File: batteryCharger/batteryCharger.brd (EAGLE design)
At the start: 44.1 x 67 mm, 73 parts, among them J1 B4P-VH(LF)(SN), Q1 SIR414DP-T1-GE3, Q2 SI7635DP-T1-GE3, Q3 SI7635DP-T1-GE3, Q4 SIR414DP-T1-GE3, Q5 SI7635DP-T1-GE3

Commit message: final board file
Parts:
- added R21, R22, R23: (no value), pot:3223W
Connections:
- removed net N$11: R5.1, RN2.7, TM1.1
- removed net N$9: R19.1, RN2.8, TM3.1
- new net ACSET_TRIM: R19.1, R23.1, RN2.8, TM3.1
- new net ISET1_TRIM: R21.1, R5.1, RN2.7, TM1.1
- net ACSET: now also R23.2
- net GND: now also R21.3, R22.3, R23.3
- net ISET1: now also R21.2
- net ISET2: now also R22.2
- net VREF: now also R22.1
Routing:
- net N$9: track 35.3 -> 0.00 mm, vias 2 -> 0
- net ISET1_TRIM: track 0.00 -> 29.2 mm
- net N$11: track 27.5 -> 0.00 mm
- net ACSET_TRIM: track 0.00 -> 24.1 mm
- net GND: track 11.7 -> 13.1 mm, vias 120 -> 122
- net ISET1: track 38.6 -> 39.2 mm
- net VREF: track 111.8 -> 111.3 mm

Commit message: v2 with bug fixses
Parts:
- removed D2, D3: (no value), SparkFun-LED:LED-1206
- added DONE, PG: (no value), SparkFun-LED:LED-1206
- added R24: 10k, SparkFun-Resistors:0603
- moved U$3 9.60 mm to (3.30, 7.49)
- moved U$2 1.20 mm to (36.4, 4.06)
- moved R4 1.02 mm to (38.0, 13.3)
- moved Q5 0.92 mm to (17.7, 55.8), turned to 0 degrees
- moved D4 0.76 mm to (31.4, 36.6)
- moved Q3 0.67 mm to (23.0, 35.5), turned to 90 degrees
- moved Q1 0.57 mm to (18.4, 50.1)
- moved C7 0.51 mm to (28.8, 39.9)
- moved R7 0.46 mm to (21.6, 21.9)
- moved Q2 0.45 mm to (23.0, 27.9), turned to 270 degrees
- moved R8 0.38 mm to (29.0, 38.1)
- moved R14 0.36 mm to (38.0, 23.9)
- moved R1 0.28 mm to (28.8, 56.6)
- moved R5 0.25 mm to (38.0, 11.2)
- moved C6 0.25 mm to (24.0, 21.1)
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- renumbered D1 to CHARGING
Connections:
- removed net N$19: C5.1, Q2.5, Q2.6, Q2.7, Q2.8, Q2.9, Q3.5, Q3.6, Q3.7, Q3.8, Q3.9, R8.1, RN2.5
- new net N$11: C5.1, Q2.1, Q2.2, Q2.3, Q3.1, Q3.2, Q3.3, R8.1, RN2.5
- net ADAPTER: now also Q2.5, Q2.6, Q2.7, Q2.8, Q2.9; no longer Q2.1, Q2.2, Q2.3
- net GND: now also R24.2
- net N$10: now also R24.1
- net N$13: now also Q3.5, Q3.6, Q3.7, Q3.8, Q3.9; no longer Q3.1, Q3.2, Q3.3
- net N$5: now also DONE.A; no longer D2.A
- net N$6: now also PG.A; no longer D3.A
- net N$7: now also DONE.C; no longer D2.C
- net N$8: now also PG.C; no longer D3.C
- net OUTPUT: now also Q5.1, Q5.2, Q5.3; no longer Q5.5, Q5.6, Q5.7, Q5.8, Q5.9
- net PACK: now also Q5.5, Q5.6, Q5.7, Q5.8, Q5.9; no longer Q5.1, Q5.2, Q5.3
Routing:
- net N$11: track 0.00 -> 38.9 mm, vias 0 -> 2
- net N$19: track 35.4 -> 0.00 mm
- net PACK: track 85.5 -> 69.7 mm
- net ADAPTER: track 71.7 -> 57.7 mm
- net N$27: track 38.0 -> 31.1 mm, vias 2 -> 4
- net N$26: track 28.6 -> 22.2 mm
- net N$23: track 18.9 -> 21.0 mm
- net N$7: track 35.2 -> 36.6 mm
- net OUTPUT: track 45.4 -> 44.1 mm
- net N$5: track 3.06 -> 4.21 mm
- net N$17: track 28.7 -> 27.9 mm
- net N$22: track 6.28 -> 7.04 mm
- net N$21: track 2.25 -> 3.01 mm
- net N$14: track 121.9 -> 122.5 mm
- net N$6: track 2.09 -> 2.59 mm
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- added copper zone on layer 1, net N$11
- removed copper zone on layer 1, net N$19
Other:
- board text added: "INPUT C"
- board text added: "OUTPUT C"
- board text added: "V2.0"
- board text removed: "AC"
- board text removed: "CI"
- board text removed: "V1.0"

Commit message: Bug fixses
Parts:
- removed TP3, TP6: TPTP20SQ, testpad:TP20SQ
- added F2: SMD-MICRO-FUSE-BLOCK, f-lf-omniblok-s:OMNIBLOK
- R10, R9: value 10mOhm -> 0.01
- R17: value 100k -> 18k
- R18: value 30k -> 22.1k
- R19, R5: value 10k -> 18k
- R4: value 30k -> 32.4k
- moved R13 50.0 mm to (39.7, 23.9), turned to 270 degrees
- moved C15 49.4 mm to (41.4, 23.9), turned to 270 degrees
- moved C19 6.30 mm to (8.46, 62.1), turned to 180 degrees
- moved C20 3.81 mm to (8.46, 60.0), turned to 180 degrees
- moved C9 2.82 mm to (34.1, 40.6), turned to 0 degrees
- moved C2 1.91 mm to (34.9, 38.0)
- moved TP1 0.54 mm to (16.3, 64.2)
- moved C11 0.13 mm to (31.3, 24.7)
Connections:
- net N$10 renamed CE
- net N$4 renamed STAT1
- net N$7 renamed STAT2
- net N$8 renamed PG
- removed net N$21: D4.C, U$1.22
- new net ISET2_TRIM: R17.1, R22.1, RN2.6, TM2.1
- new net N$9: C9.2, D4.C, U$1.22
- new net PW: C14.2, C19.1, C20.1, C3.1, F2.P$2, Q1.5, Q1.6, Q1.7, Q1.8, Q1.9, Q5.1, Q5.2, Q5.3, R20.2, R9.2, U$1.1
- net GND: no longer TP6.TP
- net N$22: no longer C9.2
- net OUTPUT: now also F2.P$1; no longer C14.2, C19.1, C20.1, C3.1, Q1.5, Q1.6, Q1.7, Q1.8, Q1.9, Q5.1, Q5.2, Q5.3, R20.2, R9.2, TP3.TP, U$1.1
- net VREF: now also RN2.3; no longer R17.1, R22.1, TM2.1
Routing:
- net N$14: track 122.5 -> 14.7 mm, vias 2 -> 0
- net OUTPUT: track 44.1 -> 0.00 mm, vias 2 -> 15
- net ISET2_TRIM: track 0.00 -> 42.8 mm
- net PW: track 0.00 -> 41.9 mm, vias 0 -> 14
- net PACK: track 69.7 -> 91.3 mm, vias 2 -> 26
- net N$9: track 0.00 -> 14.8 mm, vias 0 -> 2
- net VREF: track 111.2 -> 103.1 mm, vias 5 -> 4
- net STAT1: track 31.2 -> 36.4 mm, vias 2 -> 0
- net TSEN: track 17.7 -> 13.5 mm
- net N$24: track 21.1 -> 18.0 mm, vias 2 -> 25
- net N$21: track 3.01 -> 0.00 mm
- net STAT2: track 36.6 -> 33.6 mm
- net N$22: track 7.04 -> 4.81 mm
- net ADAPTER: track 57.7 -> 58.8 mm, vias 2 -> 21
- net PG: track 35.8 -> 36.6 mm, vias 0 -> 2
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- added copper zone on layer 16, net ADAPTER
- added copper zone on layer 16, net N$13
- added copper zone on layer 16, net N$20
- added copper zone on layer 16, net N$24
- added copper zone on layer 16, net OUTPUT
- added copper zone on layer 16, net PACK
- added copper zone on layer 1, net PW
- added copper zone on layer 16, net PW

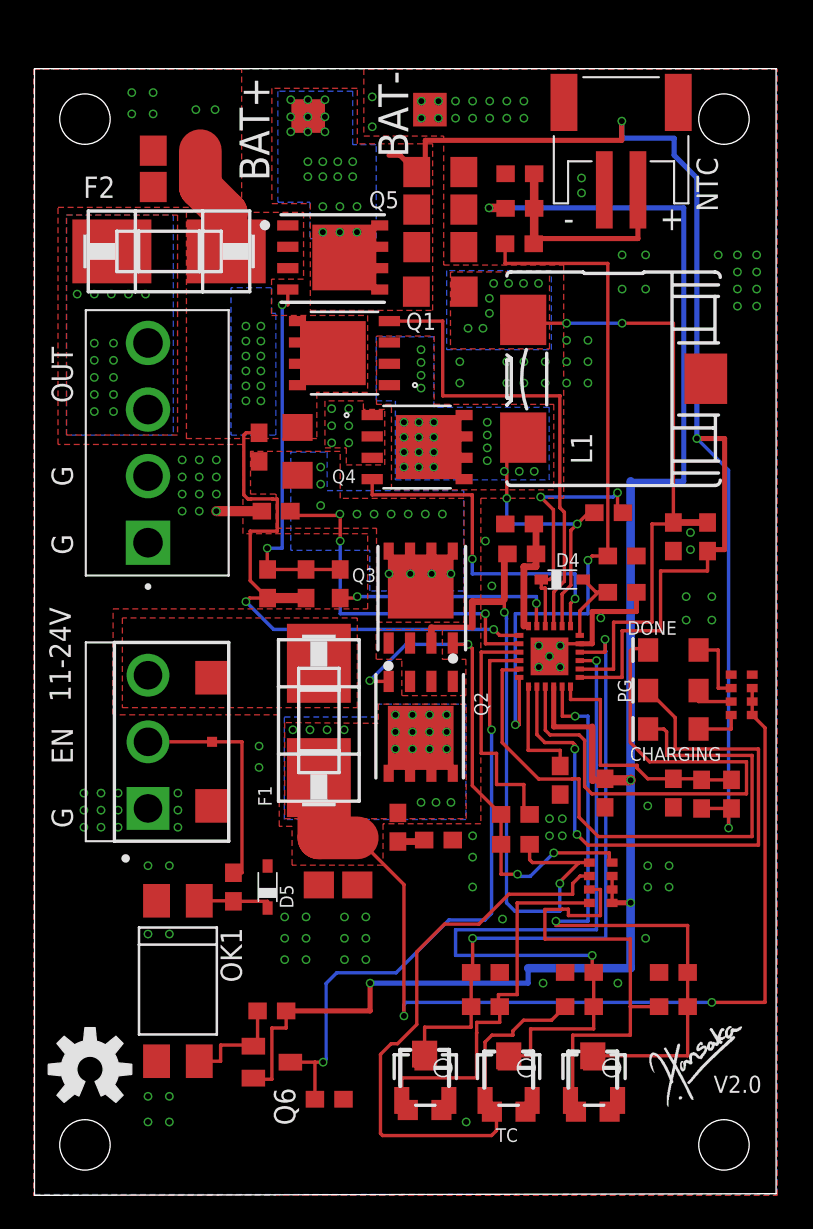
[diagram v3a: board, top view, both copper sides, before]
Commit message: Change the enable pin design
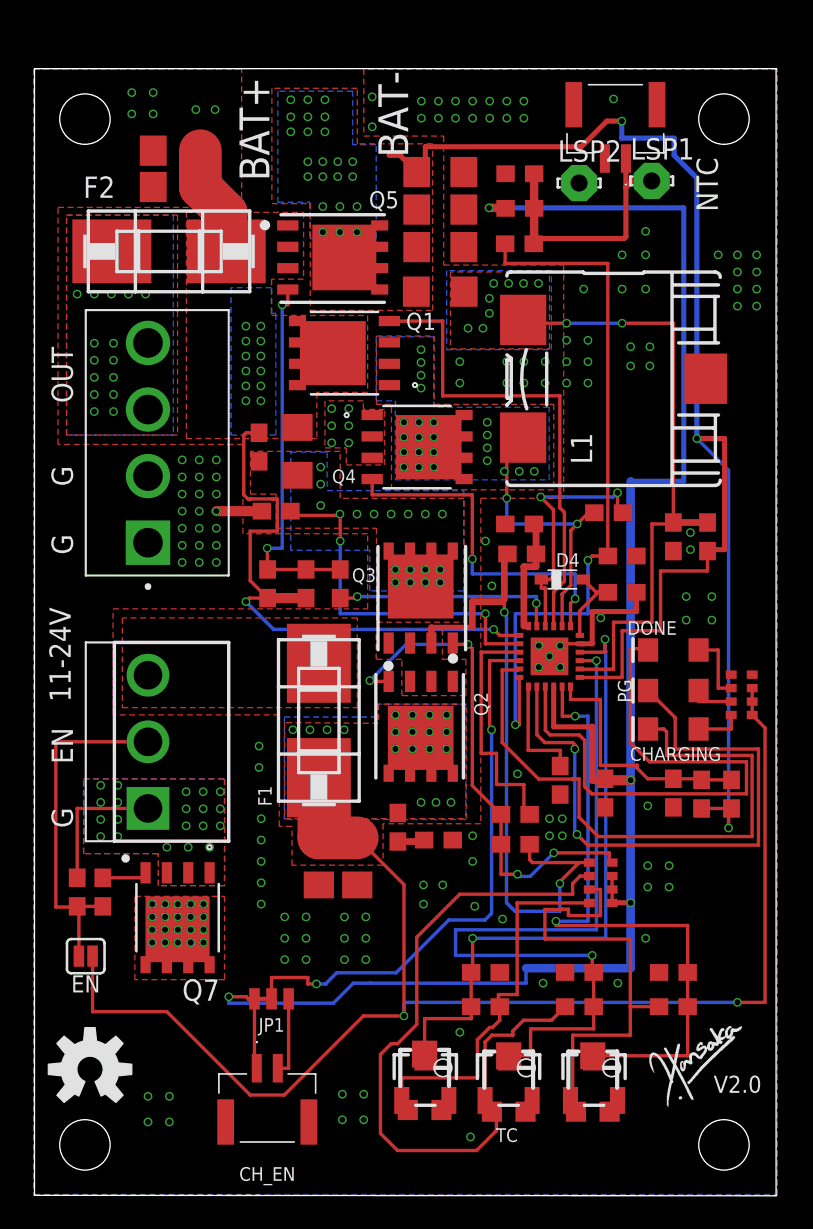
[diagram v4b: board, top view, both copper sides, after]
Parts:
- removed CN1: (no value), adafruit:JST-PH-2-SMT-RA
- removed D5: BAT60J, diode:SOD323_ST
- removed OK1: LTV816S, optocoupler:DIL4-SMD
- removed Q6: (no value), semicon-smd-ipc:SOT23
- removed R11, R24: 10k, SparkFun-Resistors:0603
- removed R15: 1.2k, SparkFun-Resistors:0603
- removed TP1, TP2, TP4, TP5: TPTP20SQ, testpad:TP20SQ
- removed TP7: TPTP06SQ, testpad:TP06SQ
- added CH_EN, CH_EN1: SM02B-GHS-TB_LF__SN_, SM02B-GHS-TB_LF__SN_:SM02BGHSTBLFSN
- added EN: JUMPER-SMT_2_NO_SILK, SparkFun-Jumpers:SMT-JUMPER_2_NO_SILK
- added JP1: JUMPER-SMT_3_1-NC_TRACE_NO-SILK, SparkFun-Jumpers:SMT-JUMPER_3_1-NC_TRACE_NO-SILK
- added LSP1, LSP2: LSP10, solpad:LSP10
- added Q7: SIR414DP-T1-GE3, SIR414DP-T1-GE3:TRANS_SQJ461EP-T1-GE3
- added R25: 1.2k, SparkFun-Resistors:0603
- added R26: 100k, SparkFun-Resistors:0603
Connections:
- removed net N$16: D5.C, OK1.1, R15.1
- new net GND_IN: Q7.1, Q7.2, Q7.3, R26.1, XA1.1
- new net N$4: Q7.4, R25.2
- net ADAPTER: now also EN.1
- net CE: now also JP1.2; no longer Q6.3, R24.1
- net EN: now also EN.2, R25.1, R26.2; no longer R15.2, TP7.TP
- net GND: now also CH_EN.3, CH_EN.4, CH_EN1.2, CH_EN1.3, CH_EN1.4, LSP2.MP, Q7.5, Q7.6, Q7.7, Q7.8, Q7.9; no longer CN1.2, D5.A, OK1.2, OK1.3, R24.2, TP2.TP, TP4.TP, XA1.1
- net INPUT: no longer TP5.TP
- net N$3: now also CH_EN.2, JP1.1; no longer OK1.4, Q6.1, R11.1
- net PACK: no longer TP1.TP
- net TSEN: now also CH_EN1.1, LSP1.MP; no longer CN1.1
- net VREF: now also CH_EN.1, JP1.3; no longer Q6.2, R11.2
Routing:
- net ADAPTER: track 58.8 -> 84.7 mm
- net GND_IN: track 0.00 -> 8.34 mm, vias 0 -> 20
- net EN: track 13.9 -> 21.2 mm
- net N$16: track 4.50 -> 0.00 mm
- net CE: track 37.3 -> 33.3 mm
- net N$4: track 0.00 -> 2.84 mm
- net TSEN: track 13.5 -> 16.3 mm
- net VREF: track 103.1 -> 105.6 mm
- net N$3: track 6.59 -> 4.77 mm
- net ISET2_TRIM: track 42.8 -> 44.1 mm
- net PACK: track 91.3 -> 90.4 mm
- net ACSET_TRIM: track 24.1 -> 23.4 mm
- net N$13: vias 16 -> 20
- net GND: vias 134 -> 166
- added copper zone on layer 1, net GND_IN
- added copper zone on layer 16, net GND_IN
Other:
- outline, holes or cut-outs redrawn
- board text added: "INPUT A"
- board text added: "OUTPUT A"
- board text removed: "INPUT C"
- board text removed: "OUTPUT C"
